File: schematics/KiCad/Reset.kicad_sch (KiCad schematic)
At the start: 15 parts, among them SW2 RESET, U11 74HC08, U13 74LS08, U14 74HC74, U16 DS1232, U17 DS1232, U2 74HC04, Y2 8MHz

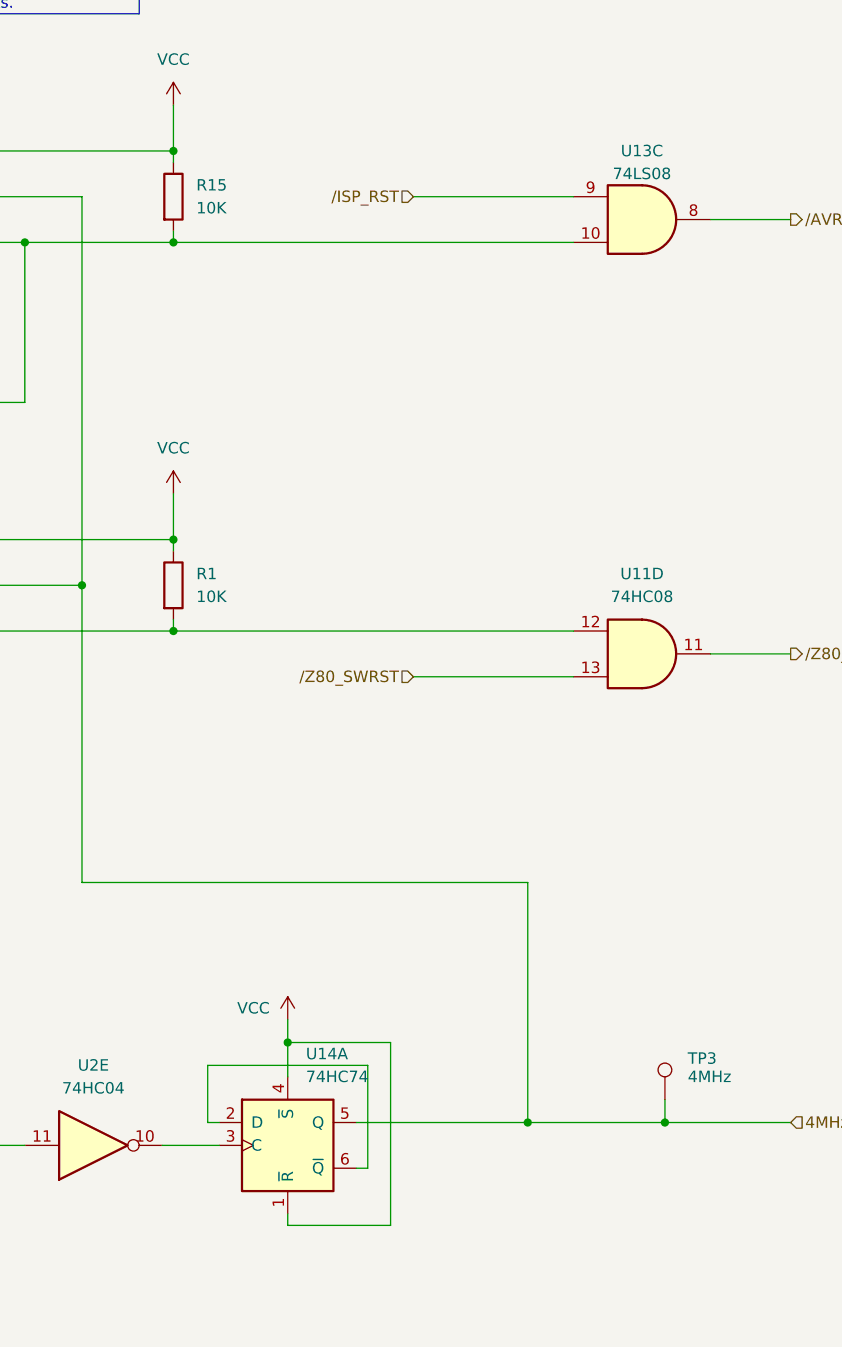
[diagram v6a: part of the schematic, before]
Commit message: Define /WAIT_0 for IOREAD and INT
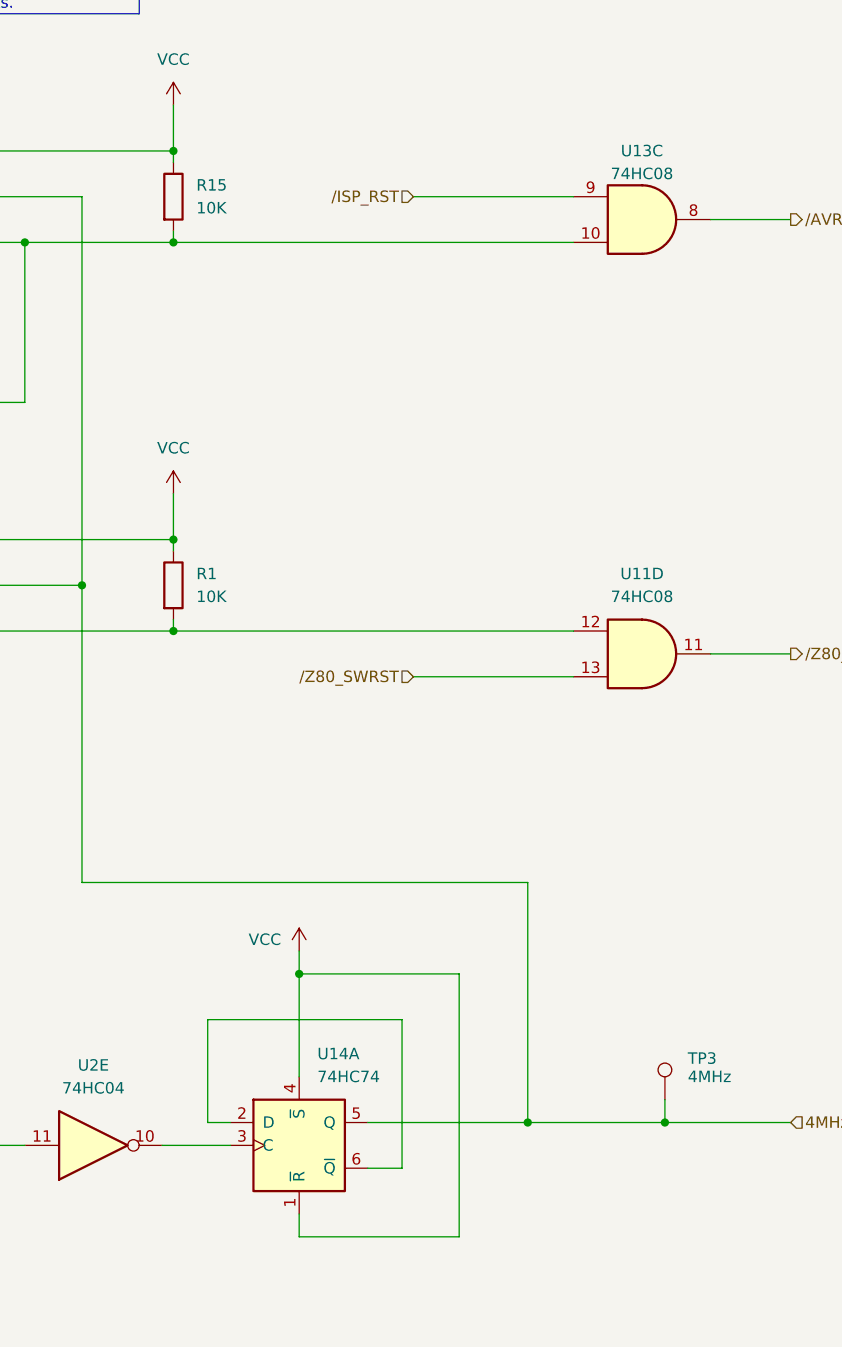
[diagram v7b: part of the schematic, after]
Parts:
- U13: value 74LS08 -> 74HC08
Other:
- moved on the sheet: U14A
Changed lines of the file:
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@@
   (title_block
     (title "Reset & Clock")
-    (date "2023-06-10")
+    (date "2023-07-16")
     (company "By 46nori")
   )
@@
   (junction (at 87.63 58.42) (diameter 0) (color 0 0 0 0)
   )
-  (junction (at 116.84 147.32) (diameter 0) (color 0 0 0 0)
-  )
   (junction (at 143.51 156.21) (diameter 0) (color 0 0 0 0)
   )
@@
   )
   (junction (at 45.72 58.42) (diameter 0) (color 0 0 0 0)
+  )
+  (junction (at 118.11 139.7) (diameter 0) (color 0 0 0 0)
   )
   (junction (at 104.14 101.6) (diameter 0) (color 0 0 0 0)
@@
     (stroke (width 0) (type default))
   )
-  (wire (pts (xy 116.84 147.32) (xy 128.27 147.32))
+  (wire (pts (xy 118.11 139.7) (xy 135.89 139.7))
     (stroke (width 0) (type default))
   )
@@
     (stroke (width 0) (type default))
   )
-  (wire (pts (xy 109.22 156.21) (xy 107.95 156.21))
-    (stroke (width 0) (type default))
-  )
-  (wire (pts (xy 102.87 158.75) (xy 109.22 158.75))
+  (wire (pts (xy 110.49 156.21) (xy 107.95 156.21))
+    (stroke (width 0) (type default))
+  )
+  (wire (pts (xy 102.87 158.75) (xy 110.49 158.75))
     (stroke (width 0) (type default))
   )
@@
     (stroke (width 0) (type default))
   )
-  (wire (pts (xy 116.84 144.78) (xy 116.84 147.32))
-    (stroke (width 0) (type default))
-  )
-  (wire (pts (xy 128.27 147.32) (xy 128.27 167.64))
+  (wire (pts (xy 118.11 137.16) (xy 118.11 139.7))
+    (stroke (width 0) (type default))
+  )
+  (wire (pts (xy 135.89 139.7) (xy 135.89 168.91))
     (stroke (width 0) (type default))
   )
@@
     (stroke (width 0) (type default))
   )
-  (wire (pts (xy 116.84 147.32) (xy 116.84 151.13))
-    (stroke (width 0) (type default))
-  )
   (wire (pts (xy 158.75 156.21) (xy 143.51 156.21))
     (stroke (width 0) (type default))
@@
     (stroke (width 0) (type default))
   )
-  (wire (pts (xy 125.73 161.29) (xy 124.46 161.29))
-    (stroke (width 0) (type default))
-  )
-  (wire (pts (xy 124.46 156.21) (xy 143.51 156.21))
+  (wire (pts (xy 129.54 161.29) (xy 125.73 161.29))
+    (stroke (width 0) (type default))
+  )
+  (wire (pts (xy 125.73 156.21) (xy 143.51 156.21))
     (stroke (width 0) (type default))
   )
@@
     (stroke (width 0) (type default))
   )
-  (wire (pts (xy 107.95 156.21) (xy 107.95 149.86))
+  (wire (pts (xy 107.95 156.21) (xy 107.95 144.78))
     (stroke (width 0) (type default))
   )
@@
     (stroke (width 0) (type default))
   )
+  (wire (pts (xy 118.11 139.7) (xy 118.11 151.13))
+    (stroke (width 0) (type default))
+  )
   (wire (pts (xy 45.72 106.68) (xy 45.72 101.6))
     (stroke (width 0) (type default))
@@
     (stroke (width 0) (type default))
   )
-  (wire (pts (xy 125.73 149.86) (xy 125.73 161.29))
+  (wire (pts (xy 129.54 144.78) (xy 129.54 161.29))
     (stroke (width 0) (type default))
   )
@@
     (stroke (width 0) (type default))
   )
-  (wire (pts (xy 116.84 167.64) (xy 116.84 166.37))
+  (wire (pts (xy 118.11 168.91) (xy 118.11 166.37))
     (stroke (width 0) (type default))
   )
@@
     (stroke (width 0) (type default))
   )
-  (wire (pts (xy 128.27 167.64) (xy 116.84 167.64))
+  (wire (pts (xy 135.89 168.91) (xy 118.11 168.91))
     (stroke (width 0) (type default))
   )
@@
     (stroke (width 0) (type default))
   )
-  (wire (pts (xy 125.73 149.86) (xy 107.95 149.86))
+  (wire (pts (xy 129.54 144.78) (xy 107.95 144.78))
     (stroke (width 0) (type default))
   )
@@
     )
   )
-  (symbol (lib_id "power:VCC") (at 116.84 144.78 0) (unit 1)
+  (symbol (lib_id "power:VCC") (at 118.11 137.16 0) (unit 1)
     (in_bom yes) (on_board yes) (dnp no)
-    (property "Reference" "#PWR044" (at 116.84 148.59 0)
-      (effects (font (size 1.27 1.27)) hide)
-    )
-    (property "Value" "VCC" (at 113.03 143.51 0)
-      (effects (font (size 1.27 1.27)))
-    )
-    (property "Footprint" "" (at 116.84 144.78 0)
-      (effects (font (size 1.27 1.27)) hide)
-    )
-    (property "Datasheet" "" (at 116.84 144.78 0)
+    (property "Reference" "#PWR044" (at 118.11 140.97 0)
+      (effects (font (size 1.27 1.27)) hide)
+    )
+    (property "Value" "VCC" (at 114.3 135.89 0)
+      (effects (font (size 1.27 1.27)))
+    )
+    (property "Footprint" "" (at 118.11 137.16 0)
+      (effects (font (size 1.27 1.27)) hide)
+    )
+    (property "Datasheet" "" (at 118.11 137.16 0)
       (effects (font (size 1.27 1.27)) hide)
     )
@@
       (effects (font (size 1.27 1.27)))
     )
-    (property "Value" "74LS08" (at 156.2017 50.8 0)
+    (property "Value" "74HC08" (at 156.2017 50.8 0)
       (effects (font (size 1.27 1.27)))
     )
@@
       (effects (font (size 1.27 1.27)) hide)
     )
-    (property "Datasheet" "http://www.ti.com/lit/gpn/sn74LS08" (at 156.21 55.88 0)
+    (property "Datasheet" "http://www.ti.com/lit/gpn/sn74HC08" (at 156.21 55.88 0)
       (effects (font (size 1.27 1.27)) hide)
     )
@@
     )
   )
-  (symbol (lib_id "74xx:74HC74") (at 116.84 158.75 0) (unit 1)
-    (in_bom yes) (on_board yes) (dnp no) (fields_autoplaced)
-    (property "Reference" "U14" (at 118.8594 148.59 0)
-      (effects (font (size 1.27 1.27)) (justify left))
-    )
-    (property "Value" "74HC74" (at 118.8594 151.13 0)
-      (effects (font (size 1.27 1.27)) (justify left))
-    )
-    (property "Footprint" "Package_DIP:DIP-14_W7.62mm_Socket" (at 116.84 158.75 0)
-      (effects (font (size 1.27 1.27)) hide)
-    )
-    (property "Datasheet" "74xx/74hc_hct74.pdf" (at 116.84 158.75 0)
-      (effects (font (size 1.27 1.27)) hide)
-    )
+  (symbol (lib_id "74xx:74HC74") (at 118.11 158.75 0) (unit 1)
+    (in_bom yes) (on_board yes) (dnp no) (fields_autoplaced)
+    (property "Reference" "U14" (at 120.1294 148.59 0)
+      (effects (font (size 1.27 1.27)) (justify left))
+    )
+    (property "Value" "74HC74" (at 120.1294 151.13 0)
+      (effects (font (size 1.27 1.27)) (justify left))
+    )
+    (property "Footprint" "Package_DIP:DIP-14_W7.62mm_Socket" (at 118.11 158.75 0)
+      (effects (font (size 1.27 1.27)) hide)
+    )
+    (property "Datasheet" "74xx/74hc_hct74.pdf" (at 118.11 158.75 0)
+      (effects (font (size 1.27 1.27)) hide)
+    )

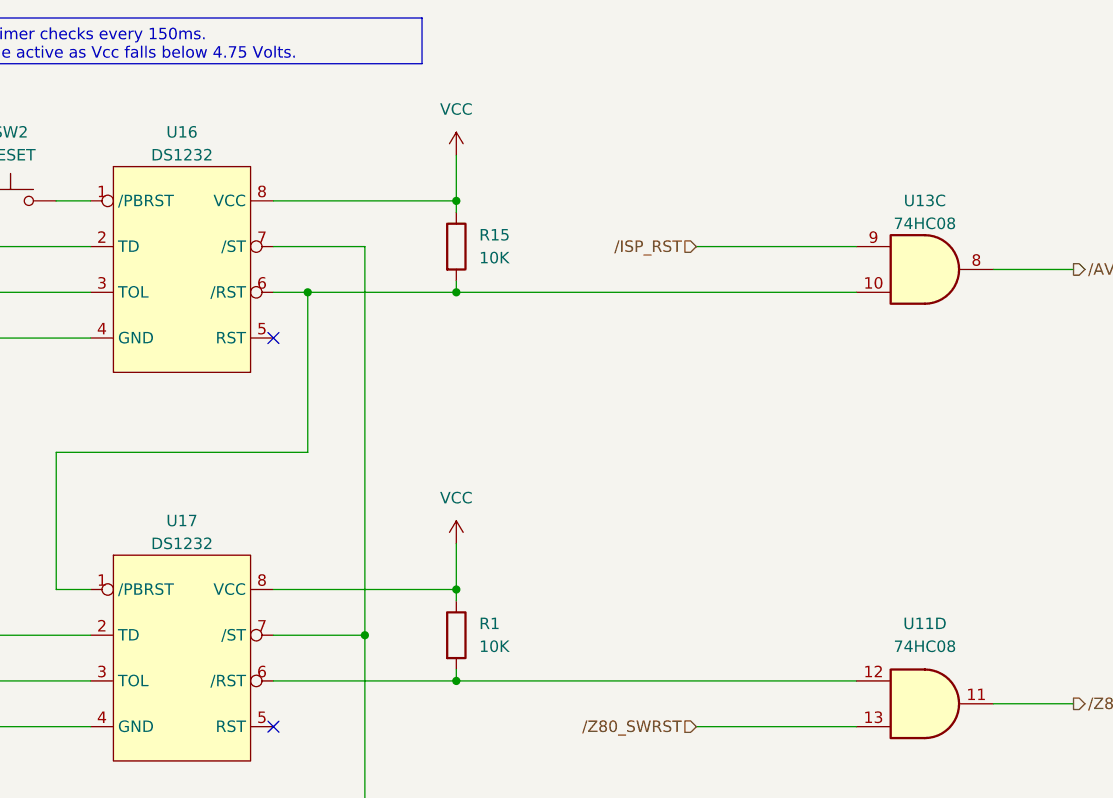
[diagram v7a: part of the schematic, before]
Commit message: Update schematics to support LED and DIP SW.
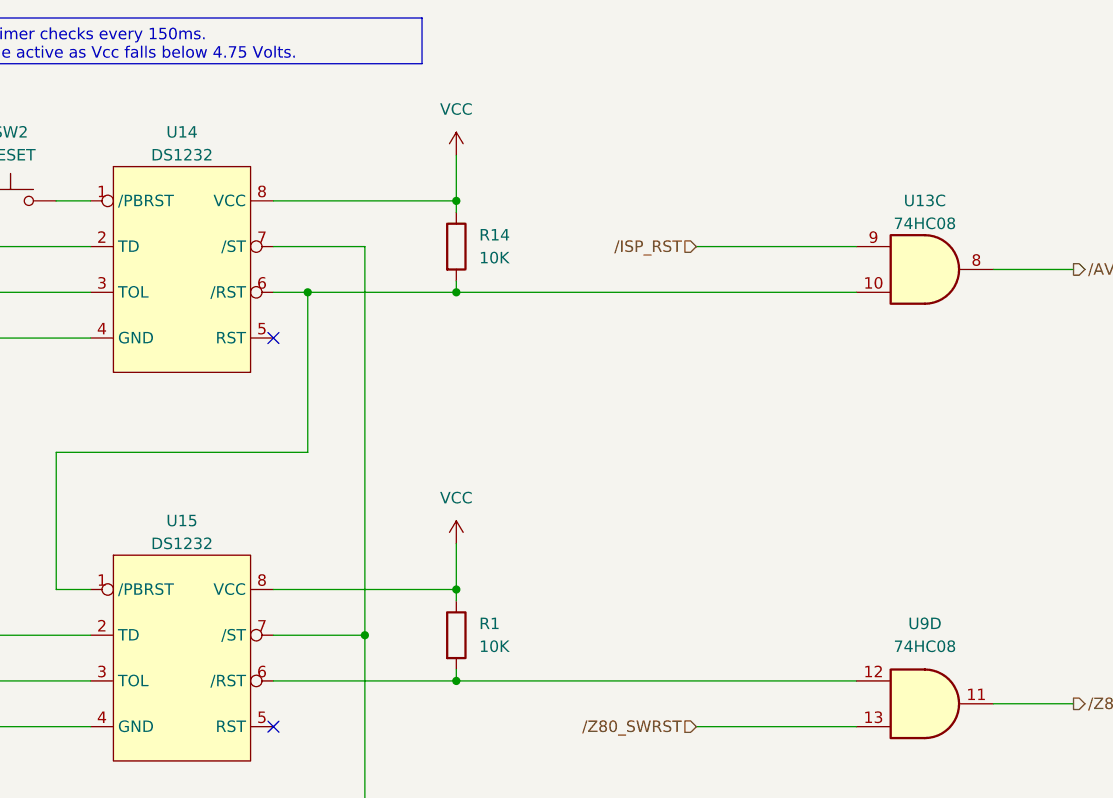
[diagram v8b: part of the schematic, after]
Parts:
- renumbered R15 to R14, U16 to U14, U17 to U15, U11 to U9
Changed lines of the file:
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@@
   (title_block
     (title "Reset & Clock")
-    (date "2023-07-16")
+    (date "2023-08-18")
     (company "By 46nori")
   )
@@
   (symbol (lib_id "power:GND") (at 45.72 114.3 0) (unit 1)
     (in_bom yes) (on_board yes) (dnp no) (fields_autoplaced)
-    (property "Reference" "#PWR067" (at 45.72 120.65 0)
+    (property "Reference" "#PWR062" (at 45.72 120.65 0)
       (effects (font (size 1.27 1.27)) hide)
     )
@@
       (project "Z80ATmega128"
         (path "/8c0ff608-9e5b-458c-8fa7-b9973ff97e88/d23d98f9-7182-4fd3-8808-8c406ff55552"
-          (reference "#PWR067") (unit 1)
+          (reference "#PWR062") (unit 1)
         )
       )
@@
         )
         (path "/8c0ff608-9e5b-458c-8fa7-b9973ff97e88/d23d98f9-7182-4fd3-8808-8c406ff55552"
-          (reference "#PWR068") (unit 1)
+          (reference "#PWR063") (unit 1)
         )
       )
@@
         )
         (path "/8c0ff608-9e5b-458c-8fa7-b9973ff97e88/d23d98f9-7182-4fd3-8808-8c406ff55552"
-          (reference "R16") (unit 1)
+          (reference "R15") (unit 1)
         )
       )
@@
   (symbol (lib_id "power:GND") (at 45.72 71.12 0) (unit 1)
     (in_bom yes) (on_board yes) (dnp no) (fields_autoplaced)
-    (property "Reference" "#PWR065" (at 45.72 77.47 0)
+    (property "Reference" "#PWR060" (at 45.72 77.47 0)
       (effects (font (size 1.27 1.27)) hide)
     )
@@
       (project "Z80ATmega128"
         (path "/8c0ff608-9e5b-458c-8fa7-b9973ff97e88/d23d98f9-7182-4fd3-8808-8c406ff55552"
-          (reference "#PWR065") (unit 1)
+          (reference "#PWR060") (unit 1)
         )
       )
@@
         )
         (path "/8c0ff608-9e5b-458c-8fa7-b9973ff97e88/d23d98f9-7182-4fd3-8808-8c406ff55552"
-          (reference "U9") (unit 3)
+          (reference "U8") (unit 3)
         )
       )
@@
         )
         (path "/8c0ff608-9e5b-458c-8fa7-b9973ff97e88/d23d98f9-7182-4fd3-8808-8c406ff55552"
-          (reference "#PWR066") (unit 1)
+          (reference "#PWR061") (unit 1)
         )
       )
@@
   (symbol (lib_id "46nori_Library:DS1232") (at 73.66 85.09 0) (unit 1)
     (in_bom yes) (on_board yes) (dnp no)
-    (property "Reference" "U17" (at 73.66 83.82 0)
+    (property "Reference" "U15" (at 73.66 83.82 0)
       (effects (font (size 1.27 1.27)))
     )
@@
       (project "Z80ATmega128"
         (path "/8c0ff608-9e5b-458c-8fa7-b9973ff97e88/d23d98f9-7182-4fd3-8808-8c406ff55552"
-          (reference "U17") (unit 1)
+          (reference "U15") (unit 1)
         )
       )
@@
         )
         (path "/8c0ff608-9e5b-458c-8fa7-b9973ff97e88/d23d98f9-7182-4fd3-8808-8c406ff55552"
-          (reference "R17") (unit 1)
+          (reference "R16") (unit 1)
         )
       )
@@
   (symbol (lib_id "Device:R") (at 104.14 53.34 0) (unit 1)
     (in_bom yes) (on_board yes) (dnp no) (fields_autoplaced)
-    (property "Reference" "R15" (at 106.68 52.0699 0)
+    (property "Reference" "R14" (at 106.68 52.0699 0)
       (effects (font (size 1.27 1.27)) (justify left))
     )
@@
       (project "Z80ATmega128"
         (path "/8c0ff608-9e5b-458c-8fa7-b9973ff97e88/d23d98f9-7182-4fd3-8808-8c406ff55552"
-          (reference "R15") (unit 1)
+          (reference "R14") (unit 1)
         )
       )
@@
         )
         (path "/8c0ff608-9e5b-458c-8fa7-b9973ff97e88/d23d98f9-7182-4fd3-8808-8c406ff55552"
-          (reference "U2") (unit 4)
+          (reference "U4") (unit 4)
         )
       )
@@
         )
         (path "/8c0ff608-9e5b-458c-8fa7-b9973ff97e88/d23d98f9-7182-4fd3-8808-8c406ff55552"
-          (reference "U15") (unit 1)
+          (reference "U12") (unit 1)
         )
       )
@@
         )
         (path "/8c0ff608-9e5b-458c-8fa7-b9973ff97e88/d23d98f9-7182-4fd3-8808-8c406ff55552"
-          (reference "U2") (unit 5)
+          (reference "U4") (unit 5)
         )
       )
@@
   (symbol (lib_id "74xx:74LS08") (at 156.21 104.14 0) (unit 4)
     (in_bom yes) (on_board yes) (dnp no)
-    (property "Reference" "U11" (at 156.21 95.25 0)
+    (property "Reference" "U9" (at 156.21 95.25 0)
       (effects (font (size 1.27 1.27)))
     )
@@
       (project "Z80ATmega128"
         (path "/8c0ff608-9e5b-458c-8fa7-b9973ff97e88/d23d98f9-7182-4fd3-8808-8c406ff55552"
-          (reference "U11") (unit 4)
+          (reference "U9") (unit 4)
         )
       )
@@
   (symbol (lib_id "power:VCC") (at 104.14 43.18 0) (unit 1)
     (in_bom yes) (on_board yes) (dnp no)
-    (property "Reference" "#PWR064" (at 104.14 46.99 0)
+    (property "Reference" "#PWR059" (at 104.14 46.99 0)
       (effects (font (size 1.27 1.27)) hide)
     )
@@
       (project "Z80ATmega128"
         (path "/8c0ff608-9e5b-458c-8fa7-b9973ff97e88/d23d98f9-7182-4fd3-8808-8c406ff55552"
+          (reference "#PWR059") (unit 1)
+        )
+      )
+    )
+  )
+  (symbol (lib_id "power:GND") (at 45.72 172.72 0) (unit 1)
+    (in_bom yes) (on_board yes) (dnp no) (fields_autoplaced)
+    (property "Reference" "#PWR048" (at 45.72 179.07 0)
+      (effects (font (size 1.27 1.27)) hide)
+    )
+    (property "Value" "GND" (at 45.72 177.8 0)
+      (effects (font (size 1.27 1.27)))
+    )
+    (property "Footprint" "" (at 45.72 172.72 0)
+      (effects (font (size 1.27 1.27)) hide)
+    )
+    (property "Datasheet" "" (at 45.72 172.72 0)
+      (effects (font (size 1.27 1.27)) hide)
+    )
+    (pin "1")
+    (instances
+      (project "Z80ATmega128"
+        (path "/8c0ff608-9e5b-458c-8fa7-b9973ff97e88"
+          (reference "#PWR048") (unit 1)
+        )
+        (path "/8c0ff608-9e5b-458c-8fa7-b9973ff97e88/d23d98f9-7182-4fd3-8808-8c406ff55552"
           (reference "#PWR064") (unit 1)
         )
@@
     )
   )
-  (symbol (lib_id "power:GND") (at 45.72 172.72 0) (unit 1)
-    (in_bom yes) (on_board yes) (dnp no) (fields_autoplaced)
-    (property "Reference" "#PWR048" (at 45.72 179.07 0)
-      (effects (font (size 1.27 1.27)) hide)
-    )
-    (property "Value" "GND" (at 45.72 177.8 0)
-      (effects (font (size 1.27 1.27)))
-    )
-    (property "Footprint" "" (at 45.72 172.72 0)
-      (effects (font (size 1.27 1.27)) hide)
-    )
-    (property "Datasheet" "" (at 45.72 172.72 0)
-      (effects (font (size 1.27 1.27)) hide)
-    )
-    (pin "1")
-    (instances
-      (project "Z80ATmega128"
-        (path "/8c0ff608-9e5b-458c-8fa7-b9973ff97e88"
-          (reference "#PWR048") (unit 1)
-        )
-        (path "/8c0ff608-9e5b-458c-8fa7-b9973ff97e88/d23d98f9-7182-4fd3-8808-8c406ff55552"
-          (reference "#PWR069") (unit 1)
-        )
-      )
-    )
-  )
   (symbol (lib_id "Switch:SW_Push") (at 54.61 48.26 0) (unit 1)
     (in_bom yes) (on_board yes) (dnp no) (fields_autoplaced)
@@
   (symbol (lib_id "46nori_Library:DS1232") (at 73.66 41.91 0) (unit 1)
     (in_bom yes) (on_board yes) (dnp no) (fields_autoplaced)
-    (property "Reference" "U16" (at 73.66 40.64 0)
+    (property "Reference" "U14" (at 73.66 40.64 0)
       (effects (font (size 1.27 1.27)))
     )
@@
       (project "Z80ATmega128"
         (path "/8c0ff608-9e5b-458c-8fa7-b9973ff97e88/d23d98f9-7182-4fd3-8808-8c406ff55552"
-          (reference "U16") (unit 1)
+          (reference "U14") (unit 1)
         )
       )
@@
         )
         (path "/8c0ff608-9e5b-458c-8fa7-b9973ff97e88/d23d98f9-7182-4fd3-8808-8c406ff55552"
-          (reference "#PWR070") (unit 1)
+          (reference "#PWR065") (unit 1)
         )
       )
@@
         )
         (path "/8c0ff608-9e5b-458c-8fa7-b9973ff97e88/d23d98f9-7182-4fd3-8808-8c406ff55552"
-          (reference "R18") (unit 1)
-        )
-      )
+          (reference "R17") (unit 1)
+        )
+      )
